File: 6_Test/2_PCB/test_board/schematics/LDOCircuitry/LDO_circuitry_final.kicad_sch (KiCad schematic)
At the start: 6 parts

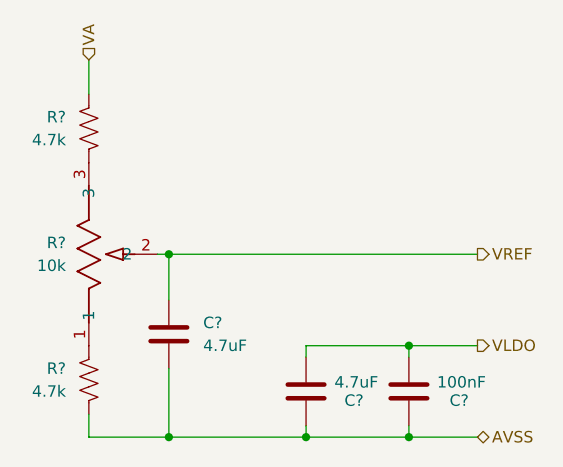
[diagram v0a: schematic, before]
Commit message: Revert "Corrections to schematic 11_20_24"
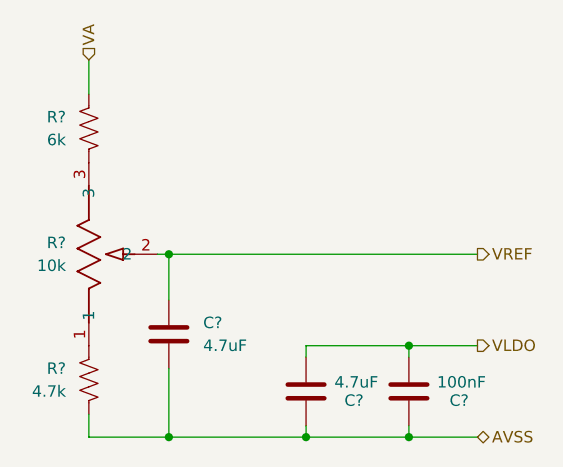
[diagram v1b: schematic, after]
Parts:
- R?: value 4.7k -> 6k
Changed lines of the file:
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@@
 				)
 			)
-			(project "board_main"
-				(path "/9c0580c5-7bd5-4e54-bf4c-826aa4ac3630/104c40d7-ae25-447b-8675-a765b7f78bca"
-					(reference "C8")
+			(project "LDO_circuitry_final"
+				(path "/9c0580c5-7bd5-4e54-bf4c-826aa4ac3630/104c40d7-ae25-447b-8675-a765b7f78bca"
+					(reference "C?")
 					(unit 1)
 				)
@@
 			)
 		)
-		(property "Value" "4.7k"
+		(property "Value" "6k"
 			(at 111.76 82.5499 0)
 			(effects
@@
 				)
 			)
-			(project "board_main"
-				(path "/9c0580c5-7bd5-4e54-bf4c-826aa4ac3630/104c40d7-ae25-447b-8675-a765b7f78bca"
-					(reference "R7")
+			(project "LDO_circuitry_final"
+				(path "/9c0580c5-7bd5-4e54-bf4c-826aa4ac3630/104c40d7-ae25-447b-8675-a765b7f78bca"
+					(reference "R?")
 					(unit 1)
 				)
@@
 				)
 			)
-			(project "board_main"
-				(path "/9c0580c5-7bd5-4e54-bf4c-826aa4ac3630/104c40d7-ae25-447b-8675-a765b7f78bca"
-					(reference "C9")
+			(project "LDO_circuitry_final"
+				(path "/9c0580c5-7bd5-4e54-bf4c-826aa4ac3630/104c40d7-ae25-447b-8675-a765b7f78bca"
+					(reference "C?")
 					(unit 1)
 				)
@@
 				)
 			)
-			(project "board_main"
-				(path "/9c0580c5-7bd5-4e54-bf4c-826aa4ac3630/104c40d7-ae25-447b-8675-a765b7f78bca"
-					(reference "C7")
+			(project "LDO_circuitry_final"
+				(path "/9c0580c5-7bd5-4e54-bf4c-826aa4ac3630/104c40d7-ae25-447b-8675-a765b7f78bca"
+					(reference "C?")
 					(unit 1)
 				)
@@
 				)
 			)
-			(project "board_main"
-				(path "/9c0580c5-7bd5-4e54-bf4c-826aa4ac3630/104c40d7-ae25-447b-8675-a765b7f78bca"
-					(reference "R8")
+			(project "LDO_circuitry_final"
+				(path "/9c0580c5-7bd5-4e54-bf4c-826aa4ac3630/104c40d7-ae25-447b-8675-a765b7f78bca"
+					(reference "R?")
 					(unit 1)
 				)
@@
 				)
 			)
-			(project "board_main"
-				(path "/9c0580c5-7bd5-4e54-bf4c-826aa4ac3630/104c40d7-ae25-447b-8675-a765b7f78bca"
-					(reference "R9")
-					(unit 1)
-				)
+			(project "LDO_circuitry_final"
+				(path "/9c0580c5-7bd5-4e54-bf4c-826aa4ac3630/104c40d7-ae25-447b-8675-a765b7f78bca"
+					(reference "R?")
+					(unit 1)
+				)

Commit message: Corrections to schematic 11_20_24
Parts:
- R?: value 6k -> 4.7k
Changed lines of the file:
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@@
 				)
 			)
-			(project "LDO_circuitry_final"
-				(path "/9c0580c5-7bd5-4e54-bf4c-826aa4ac3630/104c40d7-ae25-447b-8675-a765b7f78bca"
-					(reference "C?")
+			(project "board_main"
+				(path "/9c0580c5-7bd5-4e54-bf4c-826aa4ac3630/104c40d7-ae25-447b-8675-a765b7f78bca"
+					(reference "C8")
 					(unit 1)
 				)
@@
 			)
 		)
-		(property "Value" "6k"
+		(property "Value" "4.7k"
 			(at 111.76 82.5499 0)
 			(effects
@@
 				)
 			)
-			(project "LDO_circuitry_final"
-				(path "/9c0580c5-7bd5-4e54-bf4c-826aa4ac3630/104c40d7-ae25-447b-8675-a765b7f78bca"
-					(reference "R?")
+			(project "board_main"
+				(path "/9c0580c5-7bd5-4e54-bf4c-826aa4ac3630/104c40d7-ae25-447b-8675-a765b7f78bca"
+					(reference "R7")
 					(unit 1)
 				)
@@
 				)
 			)
-			(project "LDO_circuitry_final"
-				(path "/9c0580c5-7bd5-4e54-bf4c-826aa4ac3630/104c40d7-ae25-447b-8675-a765b7f78bca"
-					(reference "C?")
+			(project "board_main"
+				(path "/9c0580c5-7bd5-4e54-bf4c-826aa4ac3630/104c40d7-ae25-447b-8675-a765b7f78bca"
+					(reference "C9")
 					(unit 1)
 				)
@@
 				)
 			)
-			(project "LDO_circuitry_final"
-				(path "/9c0580c5-7bd5-4e54-bf4c-826aa4ac3630/104c40d7-ae25-447b-8675-a765b7f78bca"
-					(reference "C?")
+			(project "board_main"
+				(path "/9c0580c5-7bd5-4e54-bf4c-826aa4ac3630/104c40d7-ae25-447b-8675-a765b7f78bca"
+					(reference "C7")
 					(unit 1)
 				)
@@
 				)
 			)
-			(project "LDO_circuitry_final"
-				(path "/9c0580c5-7bd5-4e54-bf4c-826aa4ac3630/104c40d7-ae25-447b-8675-a765b7f78bca"
-					(reference "R?")
+			(project "board_main"
+				(path "/9c0580c5-7bd5-4e54-bf4c-826aa4ac3630/104c40d7-ae25-447b-8675-a765b7f78bca"
+					(reference "R8")
 					(unit 1)
 				)
@@
 				)
 			)
-			(project "LDO_circuitry_final"
-				(path "/9c0580c5-7bd5-4e54-bf4c-826aa4ac3630/104c40d7-ae25-447b-8675-a765b7f78bca"
-					(reference "R?")
-					(unit 1)
-				)
+			(project "board_main"
+				(path "/9c0580c5-7bd5-4e54-bf4c-826aa4ac3630/104c40d7-ae25-447b-8675-a765b7f78bca"
+					(reference "R9")
+					(unit 1)
+				)
